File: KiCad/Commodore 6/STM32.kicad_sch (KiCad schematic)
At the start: 36 parts, among them J1 472192001, J2 FTSH-107-01-L-DV-K-A, J5 FH12-24S-0.5SH_55_, J7 FH12-22S-0.5SH55, SW3 SW_Push_Dual_x2, SW5 SW_Nidec_CAS-120A1, U1 STM32H562RIT6, U2 STM32H7A3RIT6, U3 TS3A27518EIPWRQ1

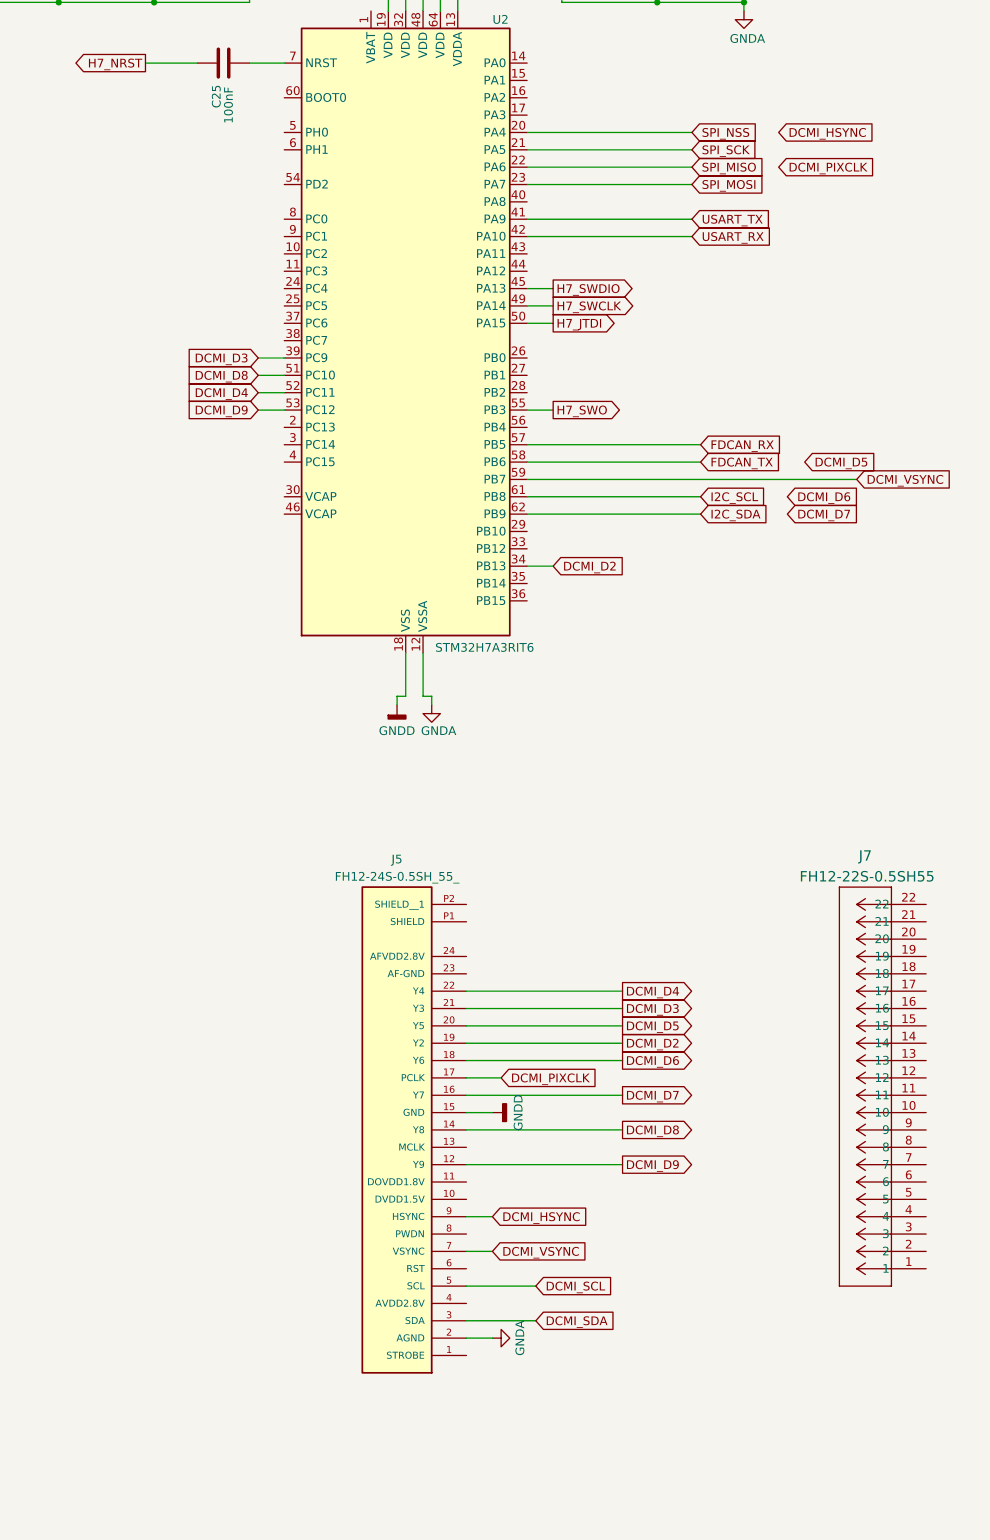
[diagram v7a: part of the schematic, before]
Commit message: Connected DCMI
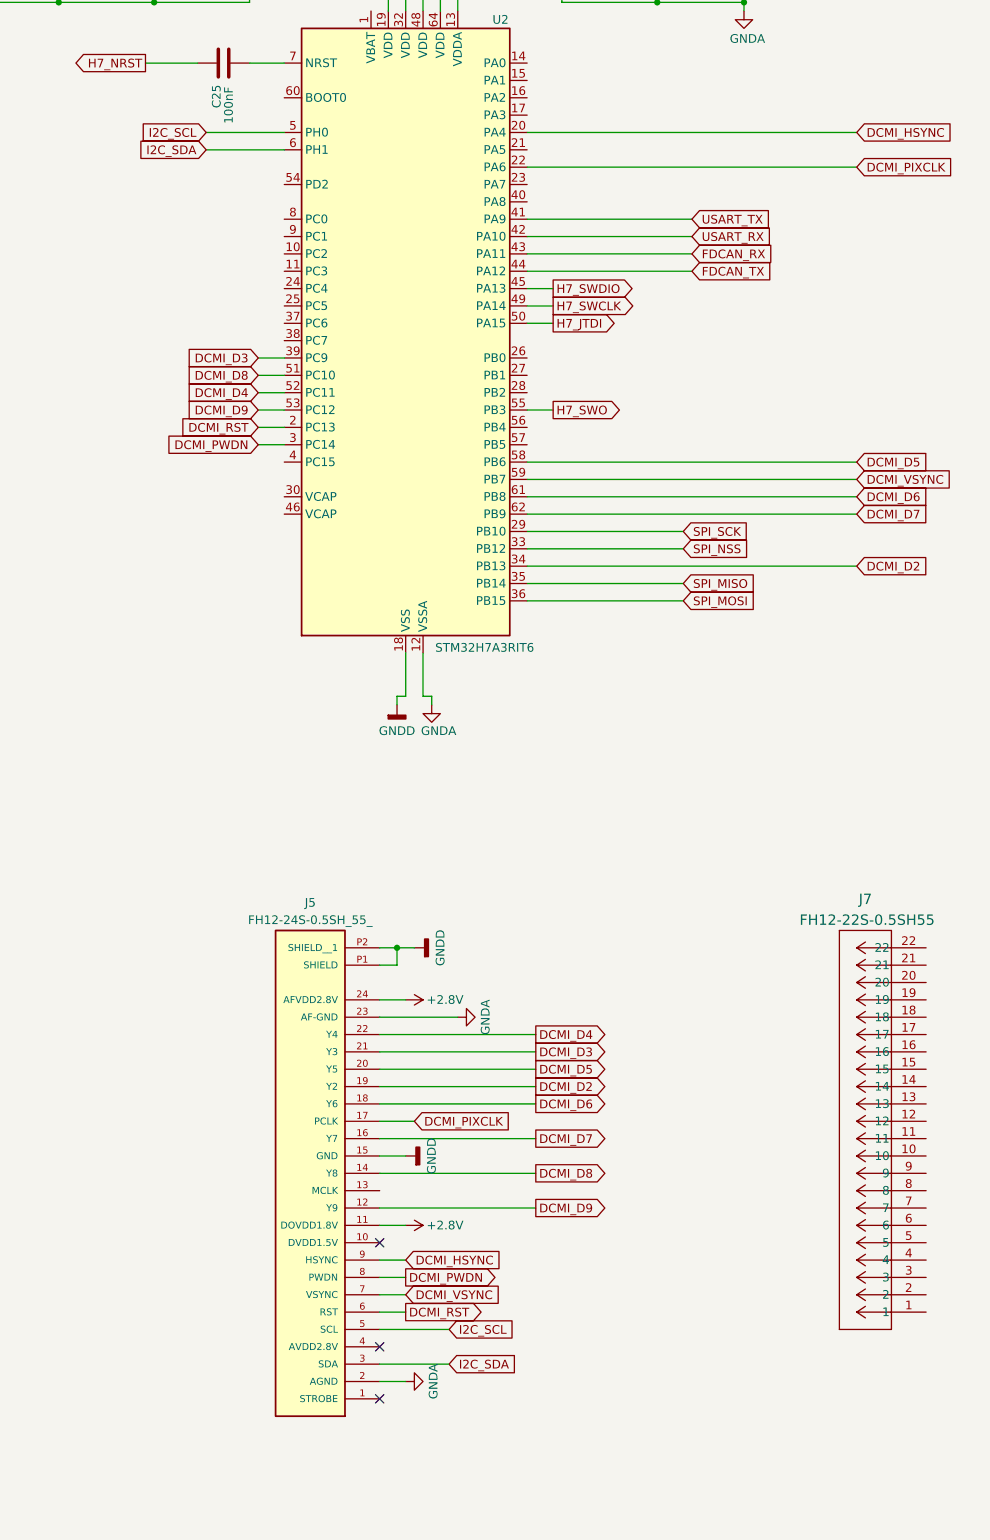
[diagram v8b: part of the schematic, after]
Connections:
- net DCMI_SCL is gone; now on net I2C_SCL: J5.5 (SCL)
- net DCMI_SDA is gone; now on net I2C_SDA: J5.3 (SDA)
- net DCMI_D5: now also U2.58 (PB6)
- net DCMI_D6: now also U2.61 (PB8)
- net DCMI_D7: now also U2.62 (PB9)
- net DCMI_HSYNC: now also U2.20 (PA4)
- net DCMI_PIXCLK: now also U2.22 (PA6)
- net FDCAN_RX: now also U2.43 (PA11); no longer U2.57 (PB5)
- net FDCAN_TX: now also U2.44 (PA12); no longer U2.58 (PB6)
- net GNDA: now also J5.23 (AF-GND)
- net GNDD: now also J5.P1 (SHIELD), J5.P2 (SHIELD__1)
- net I2C_SCL: now also U2.5 (PH0); no longer U2.61 (PB8)
- net I2C_SDA: now also U2.6 (PH1); no longer U2.62 (PB9)
- net SPI_MISO: now also U2.35 (PB14); no longer U2.22 (PA6)
- net SPI_MOSI: now also U2.36 (PB15); no longer U2.23 (PA7)
- net SPI_NSS: now also U2.33 (PB12); no longer U2.20 (PA4)
- net SPI_SCK: now also U2.29 (PB10); no longer U2.21 (PA5)
- net DCMI_RST: now reaches U2.2 (PC13)
- net DCMI_RST: now also J5.6 (RST)
- net DCMI_PWDN: now reaches U2.3 (PC14)
- net DCMI_PWDN: now also J5.8 (PWDN)
- net +2.8V: now reaches J5.11 (DOVDD1.8V)
- net +2.8V: now also J5.24 (AFVDD2.8V)
- no-connect marks 6 -> 9
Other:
- moved on the sheet: J5, J7
